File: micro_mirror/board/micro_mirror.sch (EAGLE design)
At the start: 37 parts, among them IC1 7407D, IC2 7402D, IC3 74S08D, IC4 LM324D

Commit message: Layout pretty much done, need to do silkscreen.
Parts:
- added 15V_OUT, GND, GNDA, HIN0, HIN1, HIN2, HIN3, HV_ADJ, HV_IN, HV_OUT, HV_SENSE, ID0, ID1, I_SENSE_0, I_SENSE_1, LIN0, LIN1, LIN2, LIN3, PWM_0, PWM_1, PWM_2, PWM_3, SD_0, SD_1, SD_2, SD_3, VCC, VD0, VD1, VDDA, V_SENSE_0, V_SENSE_1: (no value), modular_robotics:M04LOCK
- added C11, C25: 10nF, rcl:C-USC1206
- added C12, C13, C19: 2.2uF, rcl:C-USC1206
- added C14, C15: 22uF, rcl:C-USC1206
- added C16: 100nF 1k5V, rcl:C-USC2225K
- added C17: 180pF, rcl:C-USC1206
- added C18: 4.7uF, rcl:C-USC1206
- added C20, C21, C27, C28, C32, C33: 10nF LoESL, rcl:C-USC1206
- added C22, C29, C34: 1nF 1k5V, rcl:C-USC1206
- added C23, C24, C30, C35: 100nF, rcl:C-USC1206
- added C26, C31, C36: 470pF, rcl:C-USC1206
- added D2: (no value), diode:DIODE-SOD123
- added D3, D4, D5: BYG23T-M3, diode:DIODE-DO214AC
- added IC5: LM324D, linear:LM324D
- added J1: POWER_JACKPTH_LOCK, SparkFun-Connectors:POWER_JACKPTH_LOCK
- added L1: 2.2uH, modular_robotics:INDUCTOR
- added L2: 12uH, rcl:L-USL1812
- added R17: FUSE, rcl:R-US_R1206
- added R18: 0R, rcl:R-US_R1206
- added R19: 75k, rcl:R-US_R1206
- added R20, R25: 150k, rcl:R-US_R1206
- added R21, R39, R40: 3k3, rcl:R-US_R1206
- added R22: 2k, rcl:R-US_R1206
- added R23: 27k, rcl:R-US_R1206
- added R24: 10M, rcl:R-US_R1206
- added R26: 13k3, rcl:R-US_R1206
- added R27, R28, R44, R45, R53, R54: 100R, rcl:R-US_R1206
- added R29, R46, R55: 1M, rcl:R-US_R1206
- added R30, R35, R36, R41, R47, R56: 100k, rcl:R-US_R1206
- added R31, R33, R48, R50, R57, R59: 100M, rcl:R-US_R1206
- added R32, R34, R49, R51, R58, R60: 270k, rcl:R-US_R1206
- added R37, R38, R43, R52, R61: 1k, rcl:R-US_R1206
- added R42: FERRITE, rcl:R-US_R1206
- added U$10, U$12, U$13, U$15, U$16, U$9: HGTD1N120BNS, modular_robotics:HGTD1N120BNS
- added U$11, U$14, U$17: IR2213, modular_robotics:IR2213
- added U$5: Q50-5C, modular_robotics:Q50-5C
- added U$6: LMR64010, modular_robotics:LMR64010
- added U$7: LP2985-33, modular_robotics:LP2985-33
- added U$8: TPS62160, modular_robotics:TPS62160
- C3: value 10nF 1k5V -> 1nF 1k5V
- C5: value 10nF -> 470pF
- JP2: device modular_robotics:M04LOCK -> pinhead:PINHD-1X3
- R9: value 100R -> 1k
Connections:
- removed net ISENSE0: C10.1, R16.2
- removed net PWM0: IC2A.I0, IC3A.I0, R9.1
- removed net SD0: U$4.SD
- removed net VSENSE0: IC4B.-IN, IC4B.OUT, R13.1
- new net HIN1: HIN1.1, HIN1.2, HIN1.3, HIN1.4, IC3B.O, U$11.HIN
- new net HIN2: HIN2.1, HIN2.2, HIN2.3, HIN2.4, IC3C.O, U$14.HIN
- new net HIN3: HIN3.1, HIN3.2, HIN3.3, HIN3.4, IC3D.O, U$17.HIN
- new net HV_ADJ: HV_ADJ.1, HV_ADJ.2, HV_ADJ.3, HV_ADJ.4, R21.2, U$1.D1
- new net HV_SENSE: HV_SENSE.1, HV_SENSE.2, HV_SENSE.3, HV_SENSE.4, R23.1, R24.2, U$1.A5
- new net ID1: IC5C.+IN, ID1.1, ID1.2, ID1.3, ID1.4, R31.1, R32.2
- new net ID2: R48.1, R49.2
- new net ID3: R57.1, R58.2
- new net I_SENSE_0: C10.1, I_SENSE_0.1, I_SENSE_0.2, I_SENSE_0.3, I_SENSE_0.4, R16.2, U$1.A2
- new net I_SENSE_1: C25.1, I_SENSE_1.1, I_SENSE_1.2, I_SENSE_1.3, I_SENSE_1.4, R41.2, U$1.A4
- new net LIN1: IC2B.O, LIN1.1, LIN1.2, LIN1.3, LIN1.4, U$11.LIN
- new net LIN2: IC2C.O, LIN2.1, LIN2.2, LIN2.3, LIN2.4, U$14.LIN
- new net LIN3: IC2D.O, LIN3.1, LIN3.2, LIN3.3, LIN3.4, U$17.LIN
- new net N$12: R17.2, U$5.IN+
- new net N$17: L1.1, U$8.SW
- new net N$18: C14.1, HV_IN.1, HV_IN.2, HV_IN.3, HV_IN.4, L1.2, R17.1, R19.1, U$8.VOS
- new net N$19: C11.1, U$7.BYP
- new net N$20: R19.2, R20.2, U$8.FB
- new net N$21: D2.A, L2.2, U$6.SW
- new net N$22: R27.2, U$9.G
- new net N$23: C17.2, R25.2, R26.1, U$6.FB
- new net N$24: R21.1, R22.1, U$5.CTRL
- new net N$25: R28.2, U$10.G
- new net N$26: C20.2, R29.1, U$10.C, U$11.VS, U$9.E
- new net N$27: R27.1, U$11.HO
- new net N$28: R28.1, U$11.LO
- new net N$29: C20.1, D3.C, U$11.VB
- new net N$30: C22.1, R29.2, R30.1, R31.2
- new net N$31: IC5C.-IN, IC5C.OUT, R37.1
- new net N$32: IC5A.-IN, R35.1, R38.2
- new net N$33: IC5A.+IN, R36.1, R37.2
- new net N$34: IC5B.-IN, IC5B.OUT, R36.2
- new net N$35: IC5A.OUT, R35.2, R41.1
- new net N$36: IC5B.+IN, R39.2, R40.2
- new net N$37: C13.1, R42.2, U$7.EN, U$7.VIN
- new net N$38: IC1C.O, IC2B.I1, IC3B.I1
- new net N$39: C26.1, IC1C.I, R43.2
- new net N$40: R44.2, U$12.G
- new net N$41: R45.2, U$13.G
- new net N$42: C27.2, R46.1, U$12.E, U$13.C, U$14.VS
- new net N$43: R44.1, U$14.HO
- new net N$44: R45.1, U$14.LO
- new net N$45: C27.1, D4.C, U$14.VB
- new net N$46: C29.1, R46.2, R47.1, R48.2
- new net N$47: IC1D.O, IC2C.I1, IC3C.I1
- new net N$48: R53.2, U$15.G
- new net N$49: C31.1, IC1D.I, R52.2
- new net N$50: R54.2, U$16.G
- new net N$51: C32.2, R55.1, U$15.E, U$16.C, U$17.VS
- new net N$52: R53.1, U$17.HO
- new net N$53: R54.1, U$17.LO
- new net N$54: C32.1, D5.C, U$17.VB
- new net N$55: C34.1, R55.2, R56.1, R57.2
- new net N$56: IC1F.O, IC2D.I1, IC3D.I1
- new net N$57: C36.1, IC1F.I, R61.2
- new net PWM_0: IC2A.I0, IC3A.I0, PWM_0.1, PWM_0.2, PWM_0.3, PWM_0.4, R9.1, U$1.D7
- new net PWM_1: IC2B.I0, IC3B.I0, PWM_1.1, PWM_1.2, PWM_1.3, PWM_1.4, R43.1, U$1.D6
- new net PWM_2: IC2C.I0, IC3C.I0, PWM_2.1, PWM_2.2, PWM_2.3, PWM_2.4, R52.1, U$1.D5
- new net PWM_3: IC2D.I0, IC3D.I0, PWM_3.1, PWM_3.2, PWM_3.3, PWM_3.4, R61.1, U$1.D3
- new net SD_0: SD_0.1, SD_0.2, SD_0.3, SD_0.4, U$1.D9, U$4.SD
- new net SD_1: SD_1.1, SD_1.2, SD_1.3, SD_1.4, U$1.D4, U$11.SD
- new net SD_2: SD_2.1, SD_2.2, SD_2.3, SD_2.4, U$1.D2, U$14.SD
- new net SD_3: SD_3.1, SD_3.2, SD_3.3, SD_3.4, U$1.D0, U$17.SD
- new net VCC: C15.1, C19.1, J1.PWR, L2.1, R42.1, U$1.VIN, U$6.SHDN, U$6.VIN, U$8.EN, U$8.VIN, VCC.1, VCC.2, VCC.3, VCC.4
- new net VD1: IC5D.+IN, R33.1, R34.2, VD1.1, VD1.2, VD1.3, VD1.4
- new net VD2: R50.1, R51.2
- new net VD3: R59.1, R60.2
- new net VO2: JP2.1, R47.2, R50.2
- new net VO3: JP2.2, R56.2, R59.2
- new net V_SENSE_0: IC4D.-IN, IC4D.OUT, R13.1, U$1.A1, V_SENSE_0.1, V_SENSE_0.2, V_SENSE_0.3, V_SENSE_0.4
- new net V_SENSE_1: IC5D.-IN, IC5D.OUT, R38.1, U$1.A3, V_SENSE_1.1, V_SENSE_1.2, V_SENSE_1.3, V_SENSE_1.4
- net +15V: now also 15V_OUT.1, 15V_OUT.2, 15V_OUT.3, 15V_OUT.4, C17.1, C18.1, C21.1, C28.1, C33.1, D2.C, D3.A, D4.A, D5.A, R25.1, U$11.VCC, U$14.VCC, U$17.VCC
- net +3V3: now also C23.1, C30.1, C35.1, U$1.3V, U$11.VDD, U$14.VDD, U$17.VDD
- net GND: now also C14.2, C15.2, C16.2, C18.2, C19.2, C21.2, C22.2, C23.2, C26.2, C28.2, C29.2, C30.2, C31.2, C33.2, C34.2, C35.2, C36.2, GND.1, GND.2, GND.3, GND.4, IC1B.I, IC1E.I, J1.GND, J1.GNDBREAK, JP2.3, R18.1, R20.1, R22.2, R23.2, R26.2, R32.1, R34.1, R49.1, R51.1, R58.1, R60.1, U$1.GND1, U$1.GND2, U$10.E, U$11.COM, U$11.VSS, U$13.E, U$14.COM, U$14.VSS, U$16.E, U$17.COM, U$17.VSS, U$5.IN-, U$5.OUT-, U$6.GND, U$8.AGND, U$8.PGND
- net GNDA: now also C11.2, C12.2, C13.2, C24.2, C25.2, GNDA.1, GNDA.2, GNDA.3, GNDA.4, IC5P.V-, R18.2, R39.1, U$7.GND
- net HIN0: now also HIN0.1, HIN0.2, HIN0.3, HIN0.4
- net ID0: now also ID0.1, ID0.2, ID0.3, ID0.4
- net LIN0: now also LIN0.1, LIN0.2, LIN0.3, LIN0.4
- net N$15: now also IC4B.+IN, R15.2; no longer IC4D.+IN, R15.1
- net N$16: now also IC4B.-IN, IC4B.OUT; no longer IC4D.-IN, IC4D.OUT
- net V+: now also C16.1, HV_OUT.1, HV_OUT.2, HV_OUT.3, HV_OUT.4, R24.1, U$12.C, U$15.C, U$5.OUT+, U$9.C
- net VD0: now also IC4D.+IN, VD0.1, VD0.2, VD0.3, VD0.4; no longer IC4B.+IN
- net VDD: now also C12.1, C24.1, IC5P.V+, R15.1, R40.1, U$1.AREF, U$7.VOUT, VDDA.1, VDDA.2, VDDA.3, VDDA.4; no longer R15.2
- net VO1: now also R30.2, R33.2
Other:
- moved on the sheet: C1, C10, C2, C3, C4, C5, C6, C7, C8, C9, D1, IC1A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

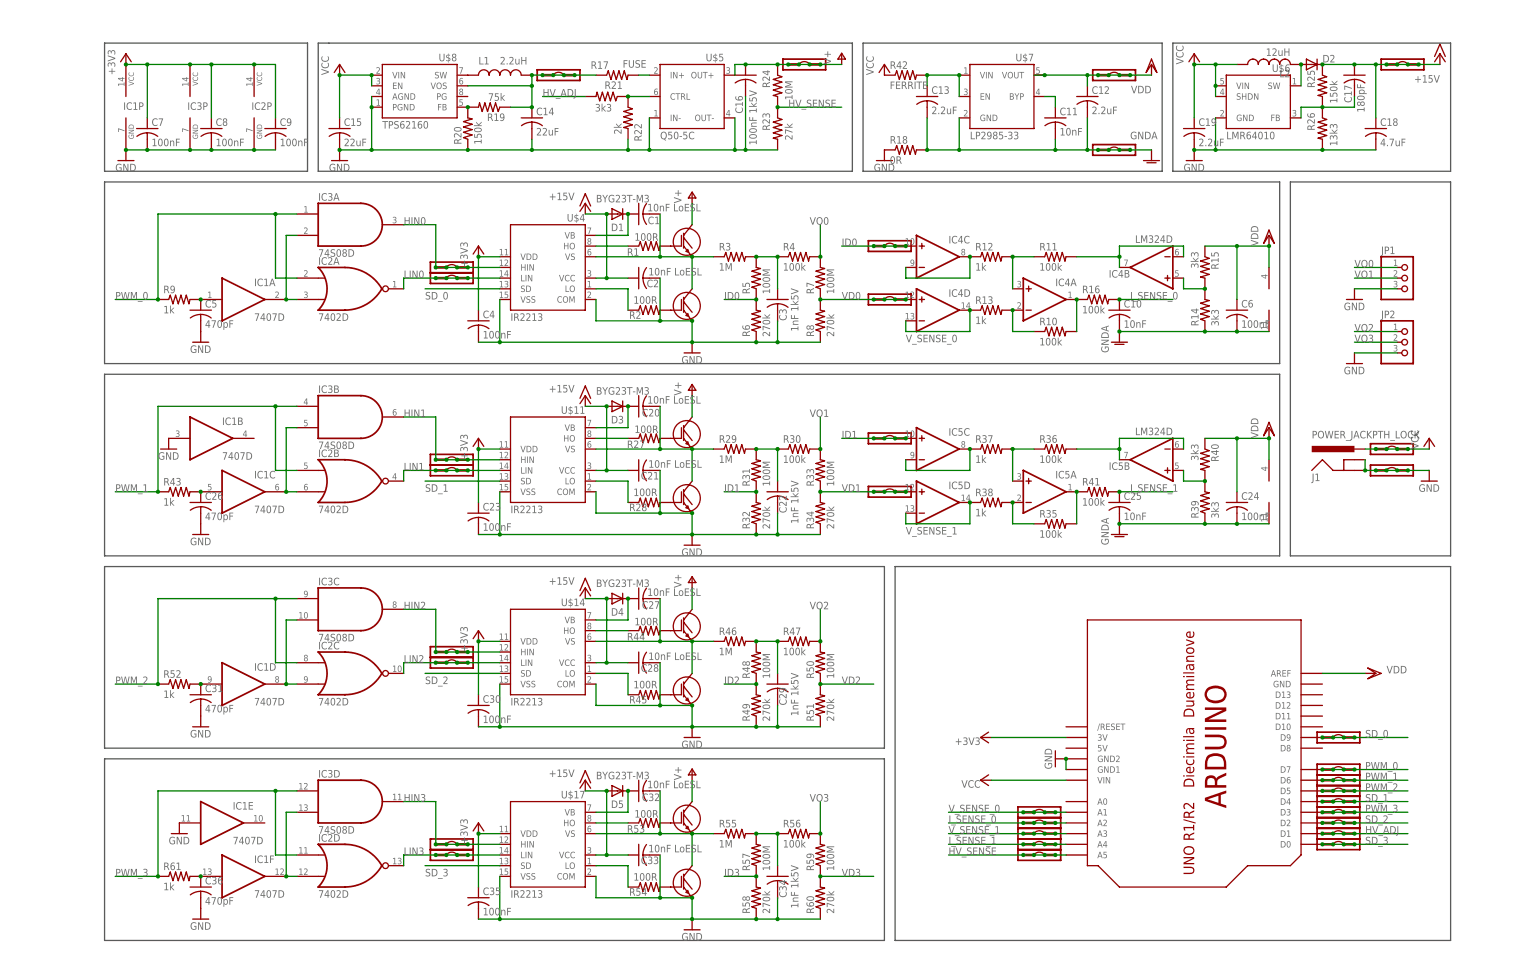
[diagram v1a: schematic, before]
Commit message: Added section labelling on schematic.
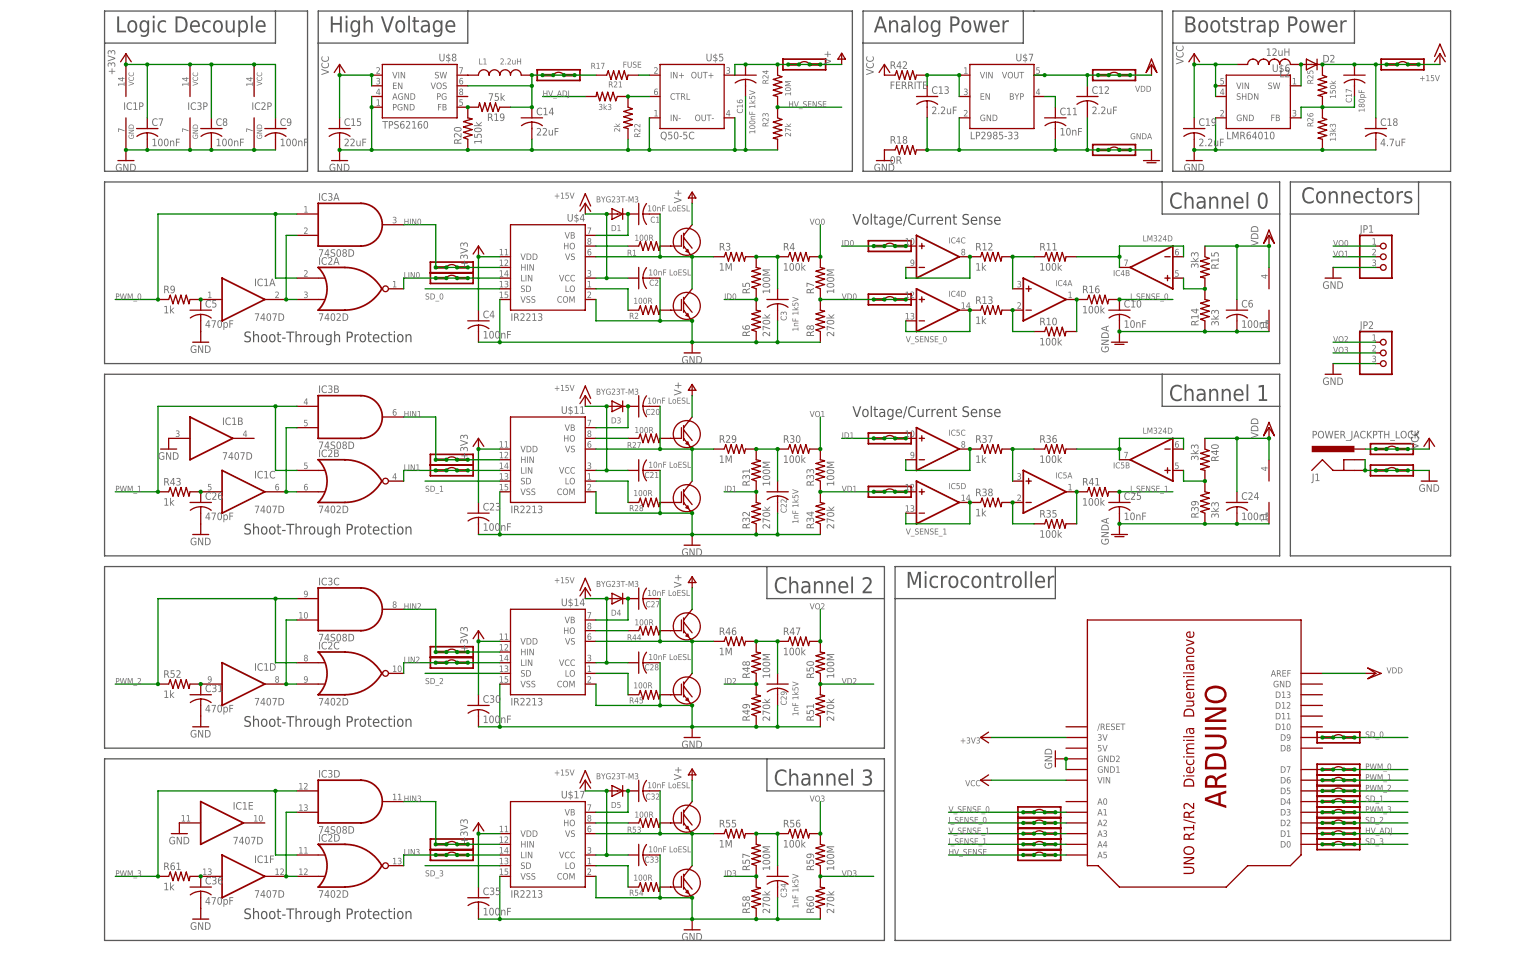
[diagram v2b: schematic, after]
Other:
- note added: "Analog Power"
- note added: "Bootstrap Power"
- note added: "Channel 0"
- note added: "Channel 1"
- note added: "Channel 2"
- note added: "Channel 3"
- note added: "Connectors"
- note added: "High Voltage"
- note added: "Logic Decouple"
- note added: "Microcontroller"
- note added: "Shoot-Through Protection"
- note added: "Voltage/Current Sense"
- moved on the sheet: JP1, JP2

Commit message: Submitted micro mirror for DFM
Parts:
- C1, C2: value 10nF LoESL -> 10nF-L
- C16: value 100nF 1k5V -> 100nF-1k5V
- C21, C28: value 10nF LoESL -> 10nF-Lo
- C3: value 1nF 1k5V -> 1nF-1k5V
- D2: value (none) -> MBR0520
- IC1: value 7407D -> 74LV7014
- IC2: value 7402D -> 74LV02
- IC3: value 74S08D -> 74LV08
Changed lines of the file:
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@@
 <part name="R1" library="rcl" deviceset="R-US_" device="R1206" value="100R"/>
 <part name="R2" library="rcl" deviceset="R-US_" device="R1206" value="100R"/>
-<part name="C1" library="rcl" deviceset="C-US" device="C1206" value="10nF LoESL"/>
-<part name="C2" library="rcl" deviceset="C-US" device="C1206" value="10nF LoESL"/>
+<part name="C1" library="rcl" deviceset="C-US" device="C1206" value="10nF-L"/>
+<part name="C2" library="rcl" deviceset="C-US" device="C1206" value="10nF-L"/>
 <part name="D1" library="diode" deviceset="DIODE-" device="DO214AC" value="BYG23T-M3"/>
 <part name="P+1" library="supply1" deviceset="+15V" device=""/>
@@
 <part name="GND1" library="supply1" deviceset="GND" device=""/>
 <part name="R3" library="rcl" deviceset="R-US_" device="R1206" value="1M"/>
-<part name="C3" library="rcl" deviceset="C-US" device="C1206" value="1nF 1k5V"/>
+<part name="C3" library="rcl" deviceset="C-US" device="C1206" value="1nF-1k5V"/>
 <part name="R4" library="rcl" deviceset="R-US_" device="R1206" value="100k"/>
 <part name="C4" library="rcl" deviceset="C-US" device="C1206" value="100nF"/>
@@
 <part name="R7" library="rcl" deviceset="R-US_" device="R1206" value="100M"/>
 <part name="R8" library="rcl" deviceset="R-US_" device="R1206" value="270k"/>
-<part name="IC1" library="74xx-us" deviceset="74*07" device="D"/>
-<part name="IC2" library="74xx-us" deviceset="74*02" device="D"/>
-<part name="IC3" library="74xx-us" deviceset="74*08" device="D" technology="S"/>
+<part name="IC1" library="74xx-us" deviceset="74*07" device="D" value="74LV7014"/>
+<part name="IC2" library="74xx-us" deviceset="74*02" device="D" value="74LV02"/>
+<part name="IC3" library="74xx-us" deviceset="74*08" device="D" technology="S" value="74LV08"/>
 <part name="R9" library="rcl" deviceset="R-US_" device="R1206" value="1k"/>
 <part name="C5" library="rcl" deviceset="C-US" device="C1206" value="470pF"/>
@@
 <part name="R23" library="rcl" deviceset="R-US_" device="R1206" value="27k"/>
 <part name="R24" library="rcl" deviceset="R-US_" device="R1206" value="10M"/>
-<part name="C16" library="rcl" deviceset="C-US" device="C2225K" value="100nF 1k5V"/>
+<part name="C16" library="rcl" deviceset="C-US" device="C2225K" value="100nF-1k5V"/>
 <part name="P+5" library="supply1" deviceset="V+" device=""/>
 <part name="HV_OUT" library="modular_robotics" deviceset="M04" device="LOCK"/>
 <part name="L2" library="rcl" deviceset="L-US" device="L1812" value="12uH"/>
-<part name="D2" library="diode" deviceset="DIODE-" device="SOD123"/>
+<part name="D2" library="diode" deviceset="DIODE-" device="SOD123" value="MBR0520"/>
 <part name="R25" library="rcl" deviceset="R-US_" device="R1206" value="150k"/>
 <part name="R26" library="rcl" deviceset="R-US_" device="R1206" value="13k3"/>
@@
 <part name="R28" library="rcl" deviceset="R-US_" device="R1206" value="100R"/>
 <part name="C20" library="rcl" deviceset="C-US" device="C1206" value="10nF LoESL"/>
-<part name="C21" library="rcl" deviceset="C-US" device="C1206" value="10nF LoESL"/>
+<part name="C21" library="rcl" deviceset="C-US" device="C1206" value="10nF-Lo"/>
 <part name="D3" library="diode" deviceset="DIODE-" device="DO214AC" value="BYG23T-M3"/>
 <part name="P+10" library="supply1" deviceset="+15V" device=""/>
@@
 <part name="R45" library="rcl" deviceset="R-US_" device="R1206" value="100R"/>
 <part name="C27" library="rcl" deviceset="C-US" device="C1206" value="10nF LoESL"/>
-<part name="C28" library="rcl" deviceset="C-US" device="C1206" value="10nF LoESL"/>
+<part name="C28" library="rcl" deviceset="C-US" device="C1206" value="10nF-Lo"/>
 <part name="D4" library="diode" deviceset="DIODE-" device="DO214AC" value="BYG23T-M3"/>
 <part name="P+12" library="supply1" deviceset="+15V" device=""/>
